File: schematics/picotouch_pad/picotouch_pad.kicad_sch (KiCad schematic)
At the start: 105 parts, among them J1 AudioJack4, SW1 SSSS811101, U1 Pico, U2 MCP73831-2-OT, X1 AFC20-S02ACA-00

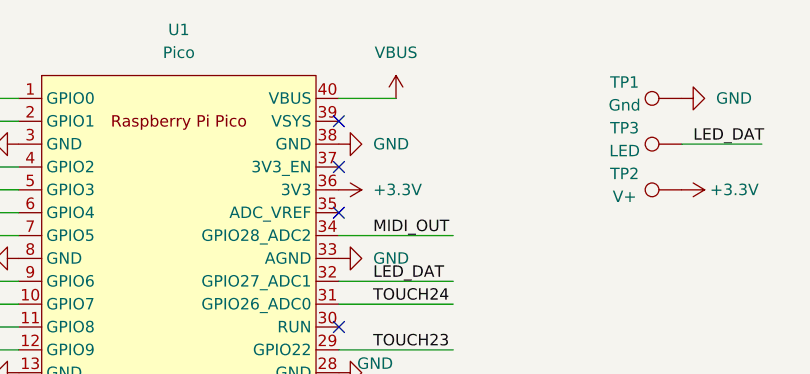
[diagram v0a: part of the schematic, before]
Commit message: one net forgot! fix +5V to VSYS
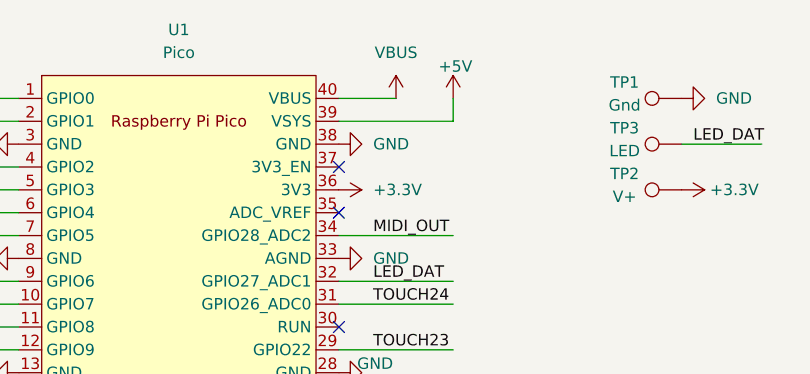
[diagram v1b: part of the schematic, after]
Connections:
- net +5V: now also U1.39 (VSYS)
- no-connect marks 9 -> 8
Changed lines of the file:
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@@
-	)
-	(no_connect
-		(at 78.74 35.56)
 	)
 	(no_connect
@@
 	(wire
 		(pts
+			(xy 78.74 35.56) (xy 91.44 35.56)
+		)
+		(stroke
+			(width 0)
+			(type default)
+		)
+	)
+	(wire
+		(pts
 			(xy 85.09 33.02) (xy 78.74 33.02)
 		)
@@
 		(pts
 			(xy 78.74 66.04) (xy 91.44 66.04)
+		)
+		(stroke
+			(width 0)
+			(type default)
+		)
+	)
+	(wire
+		(pts
+			(xy 91.44 33.02) (xy 91.44 35.56)
 		)
 		(stroke
@@
 					(unit 1)
 				)
+			)
+		)
+	)
+	(symbol
+		(lib_id "power:+5V")
+		(at 91.44 33.02 0)
+		(unit 1)
+		(exclude_from_sim no)
+		(in_bom yes)
+		(on_board yes)
+		(dnp no)
+		(property "Reference" "#PWR0127"
+			(at 91.44 36.83 0)
+			(effects
+				(font
+					(size 1.27 1.27)
+				)
+				(hide yes)
+			)
+		)
+		(property "Value" "+5V"
+			(at 91.694 29.464 0)
+			(effects
+				(font
+					(size 1.27 1.27)
+				)
+			)
+		)
+		(property "Footprint" ""
+			(at 91.44 33.02 0)
+			(effects
+				(font
+					(size 1.27 1.27)
+				)
+				(hide yes)
+			)
+		)
+		(property "Datasheet" ""
+			(at 91.44 33.02 0)
+			(effects
+				(font
+					(size 1.27 1.27)
+				)
+				(hide yes)
+			)
+		)
+		(property "Description" "Power symbol creates a global label with name \"+5V\""
+			(at 91.44 33.02 0)
+			(effects
+				(font
+					(size 1.27 1.27)
+				)
+				(hide yes)
+			)
+		)
+		(pin "1"
+		)
+		(instances
+			(project "picotouch_pad"
+				(path "/a83b8b47-e572-48e2-b6f7-0ec1c4c903c4"
+					(reference "#PWR0127")
+					(unit 1)
+				)
